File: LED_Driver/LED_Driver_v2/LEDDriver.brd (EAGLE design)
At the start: 23.9 x 16.5 mm, 14 parts, among them Q1 DMP2012SN-7, U1 LM3409HV'LM3409HV'

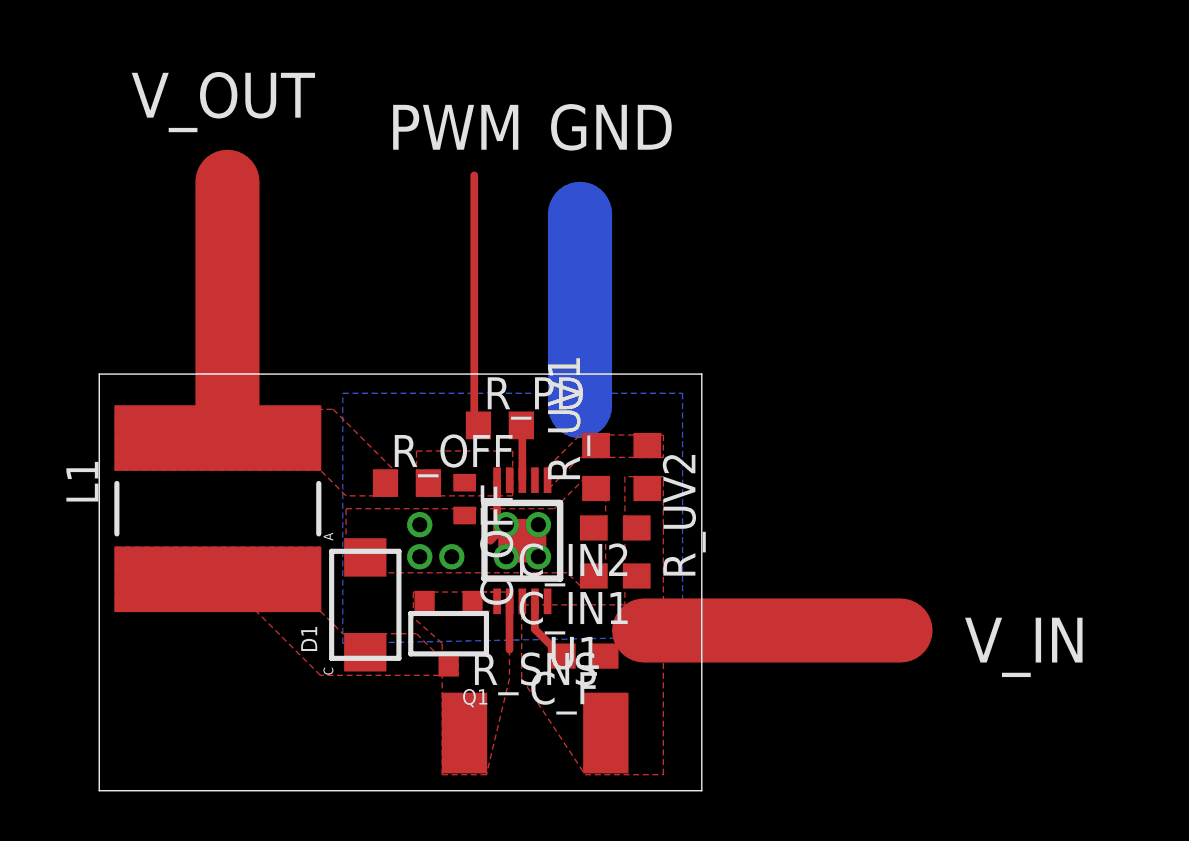
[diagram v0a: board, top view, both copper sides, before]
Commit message: Minor changes to trace placement in LED Driver v2
Minor changes to trace placement in LED Driver v2
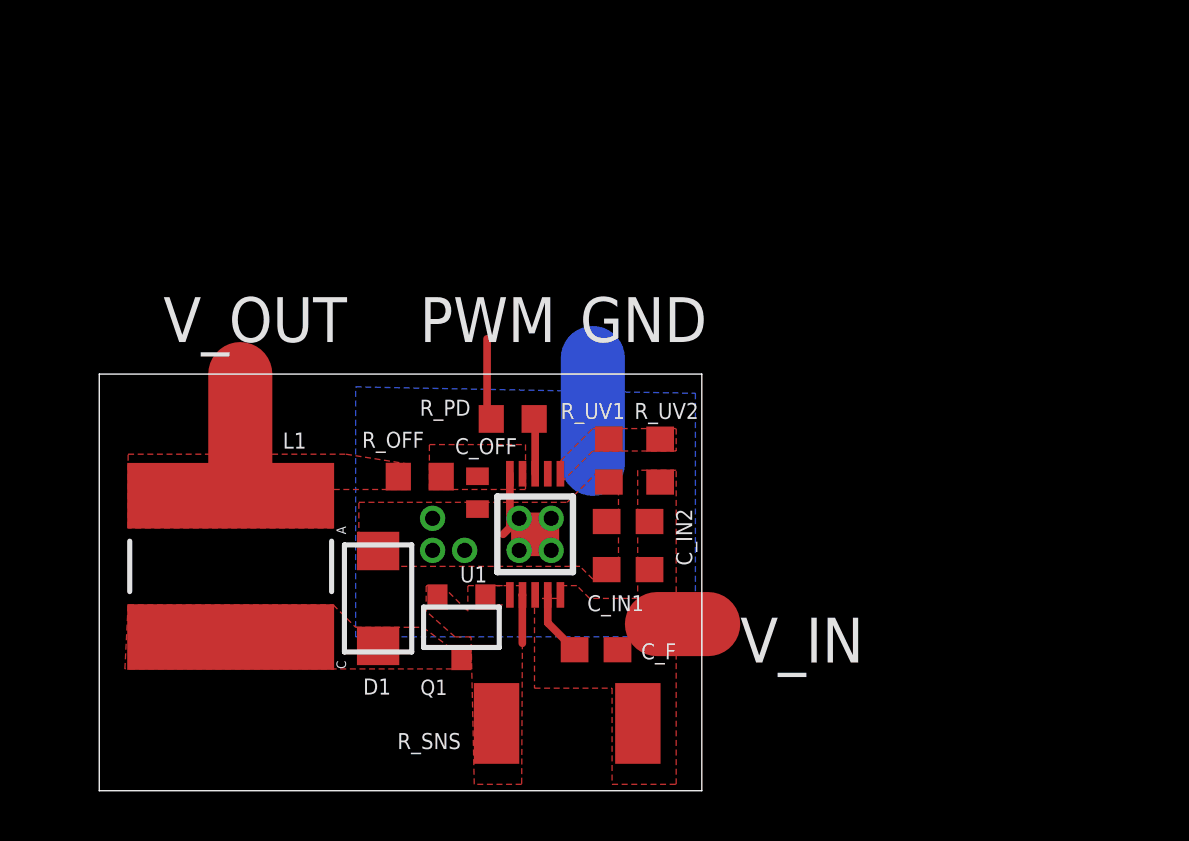
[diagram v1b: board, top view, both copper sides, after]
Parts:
- removed FRAME1: FRAME-LETTER, SparkFun-Aesthetics:CREATIVE_COMMONS
- moved L1 2.34 mm to (5.21, 8.89)
- moved R_SNS 1.33 mm to (18.5, 2.67)
- moved R_UV1 0.57 mm to (20.2, 13.1)
- moved R_UV2 0.57 mm to (22.2, 13.1)
- moved Q1 0.57 mm to (14.4, 6.48)
- moved C_OFF 0.57 mm to (15.0, 11.8)
- moved C_F 0.57 mm to (19.7, 5.59)
- moved D1 0.57 mm to (11.0, 7.62)
- moved C_IN1 0.57 mm to (21.0, 8.76)
- moved C_IN2 0.57 mm to (21.0, 10.7)
- moved R_OFF 0.57 mm to (12.7, 12.4)
- moved R_PD 0.57 mm to (16.4, 14.7)
- moved U1 0.57 mm to (17.3, 10.2)
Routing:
- net N$7: track 10.2 -> 0.00 mm
- net V_OUT: track 0.00 -> 9.42 mm
- net N$16: track 8.89 -> 0.00 mm
- net N$17: track 7.62 -> 0.00 mm
- net N$15: track 10.0 -> 3.30 mm
- net GND: track 2.51 -> 6.70 mm, vias 4 -> 7
- net V_IN: track 0.00 -> 2.03 mm
